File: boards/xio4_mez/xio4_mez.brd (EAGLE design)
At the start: 63 x 91 mm, 55 parts, among them J1 FPGA

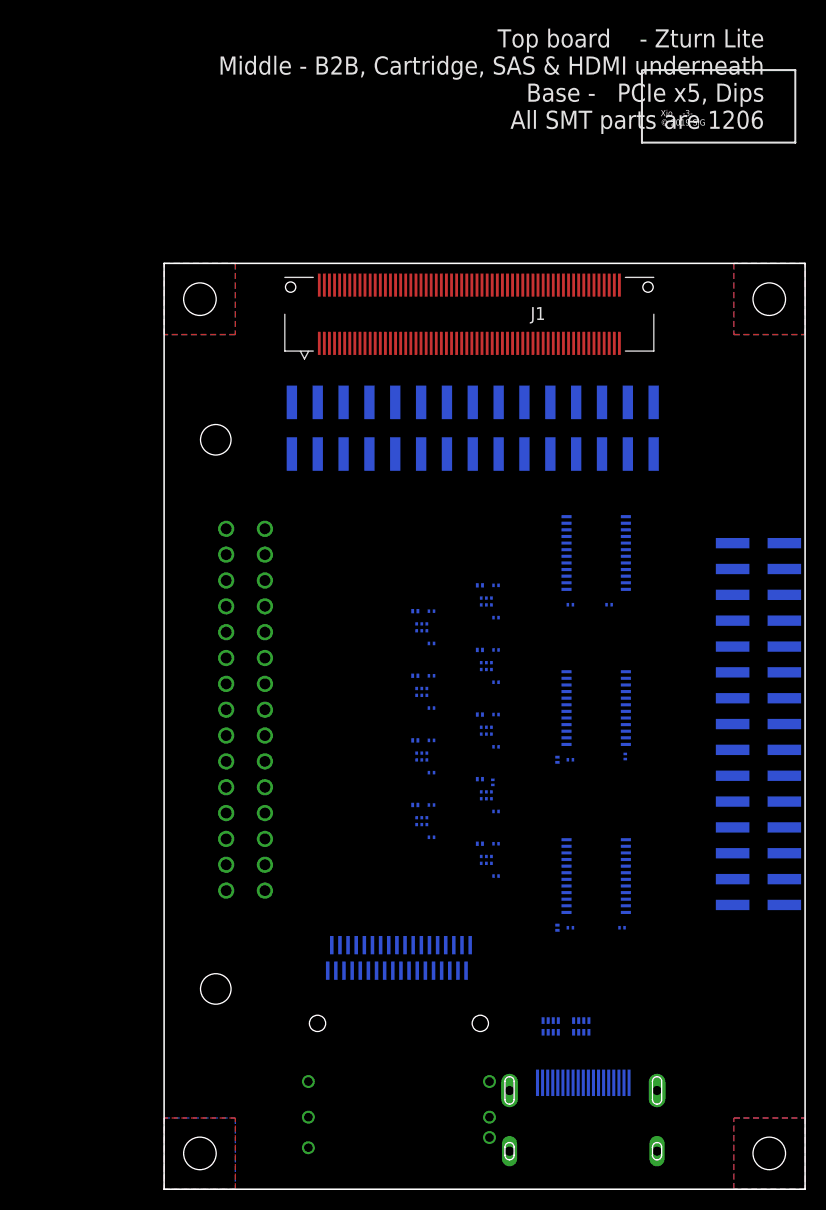
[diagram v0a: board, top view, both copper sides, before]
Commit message: Add the HDMI stage
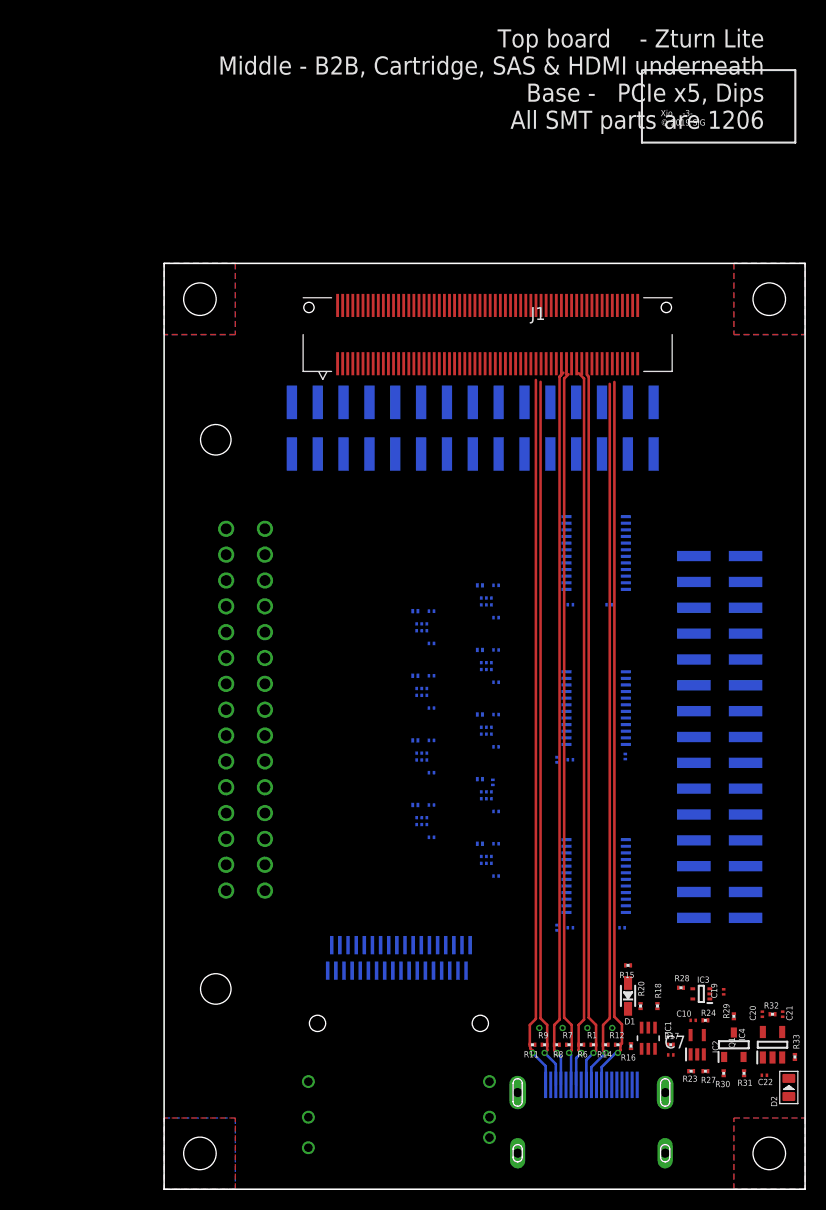
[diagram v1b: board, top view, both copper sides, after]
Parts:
- removed RN1, RN2: 49R9, samacsys:YC124FR0749R9L
- added C10, C19, C20, C21, C22, C7: 0.1uF, rcl:C0201
- added D1: RB751V40,115, microbuilder:SOD-323
- added D2: RED-0805, Seeed-LED:LED-0805
- added IC1: SN74LVC2G07DCKR, samacsys:SOT65P210X110X6N
- added IC2: SN74LVC1G07MDCKREP, samacsys:SOT65P210X110-5N
- added IC3: NL17SZ126XV5T2G, samacsys:SOTFL50P160X60-5N
- added IC4: TPS2051BDBVR, samacsys:SOT95P280X145-5N
- added Q1: SMMBT3904LT1G, samacsys:SOT96P237X111-3N
- added R1, R11, R12, R14, R6, R7, R8, R9: 49R9, rcl:R0201
- added R15: 27K, rcl:R0201
- added R16, R17: 1K5, rcl:R0201
- added R18, R20: 4K7, rcl:R0201
- added R23, R27: 100K, rcl:R0201
- added R24, R28, R30: 1K, rcl:R0201
- added R29, R31, R32: 10K, rcl:R0201
- added R33: 820R, rcl:R0201
- moved JP2 4.02 mm to (55.9, 27.9)
- moved J1 2.69 mm to (31.8, 84.0)
- moved CN1 0.82 mm to (42.0, 10.3)
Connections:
- removed net TX0_SHIELD: CN1.8
- removed net TX1_SHIELD: CN1.5
- removed net TX2_SHIELD: CN1.2
- removed net TXC_SHIELD: CN1.11
- new net HDMI_CEC: CN1.13, D1.C, J1.90
- new net HDMI_DET_IO: IC3.2, J1.84, R24.2, R27.2
- new net HDMI_OUT_EN: J1.80, R30.1, R32.2
- new net HDMI_SCL: IC1.1, J1.88, R18.2
- new net HDMI_SDA: IC1.3, J1.86, R20.2
- new net HPD: CN1.19, IC2.2, R23.2, R28.2
- new net N$1: CN1.16, IC1.6, R17.1
- new net N$10: D2.-, R33.2
- new net N$2: D1.A, R15.1
- new net N$3: CN1.15, IC1.4, R16.1
- new net N$4: IC3.1, Q1.3, R29.2
- new net N$5: IC2.4, R24.1
- new net N$6: IC3.4, R28.1
- new net N$7: Q1.1, R30.2, R31.1
- new net N$8: C21.1, IC4.4, R32.1
- new net N$9: IC4.3, R33.1
- new net V+: C22.1, C7.1, CN1.18, IC4.1, R16.2, R17.2
- net +5V: now also C20.1, IC4.5; no longer CN1.18
- net GND: now also C10.2, C19.2, C20.2, C21.2, C22.2, C7.2, CN1.11, CN1.2, CN1.5, CN1.8, IC1.2, IC2.3, IC3.3, IC4.2, Q1.2, R23.1, R27.1, R31.2
- net TX0_N: now also R1.2; no longer RN1.3
- net TX0_P: now also R6.2; no longer RN1.4
- net TX1_N: now also R7.2; no longer RN2.1
- net TX1_P: now also R8.2; no longer RN2.2
- net TX2_N: now also R9.2; no longer RN2.3
- net TX2_P: now also R11.2; no longer RN2.4
- net TXC_N: now also R12.2; no longer RN1.1
- net TXC_P: now also R14.2; no longer RN1.2
- net VCCIO: now also C10.1, C19.1, D2.+, IC1.5, IC2.5, IC3.5, R1.1, R11.1, R12.1, R14.1, R15.2, R18.1, R20.1, R29.1, R6.1, R7.1, R8.1, R9.1; no longer RN1.5, RN1.6, RN1.7, RN1.8, RN2.5, RN2.6, RN2.7, RN2.8
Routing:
- net TX0_P: track 0.00 -> 70.7 mm, vias 0 -> 1
- net TX1_P: track 0.00 -> 70.6 mm, vias 0 -> 1
- net TX1_N: track 0.00 -> 70.5 mm, vias 0 -> 1
- net TX0_N: track 0.00 -> 70.5 mm, vias 0 -> 1
- net TXC_N: track 0.00 -> 70.3 mm, vias 0 -> 1
- net TX2_P: track 0.00 -> 70.2 mm, vias 0 -> 1
- net TX2_N: track 0.00 -> 69.9 mm, vias 0 -> 1
- net TXC_P: track 0.00 -> 69.9 mm, vias 0 -> 1

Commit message: Use the corrected footprint for the Mezzanine board, and route the HDMI critical signals.
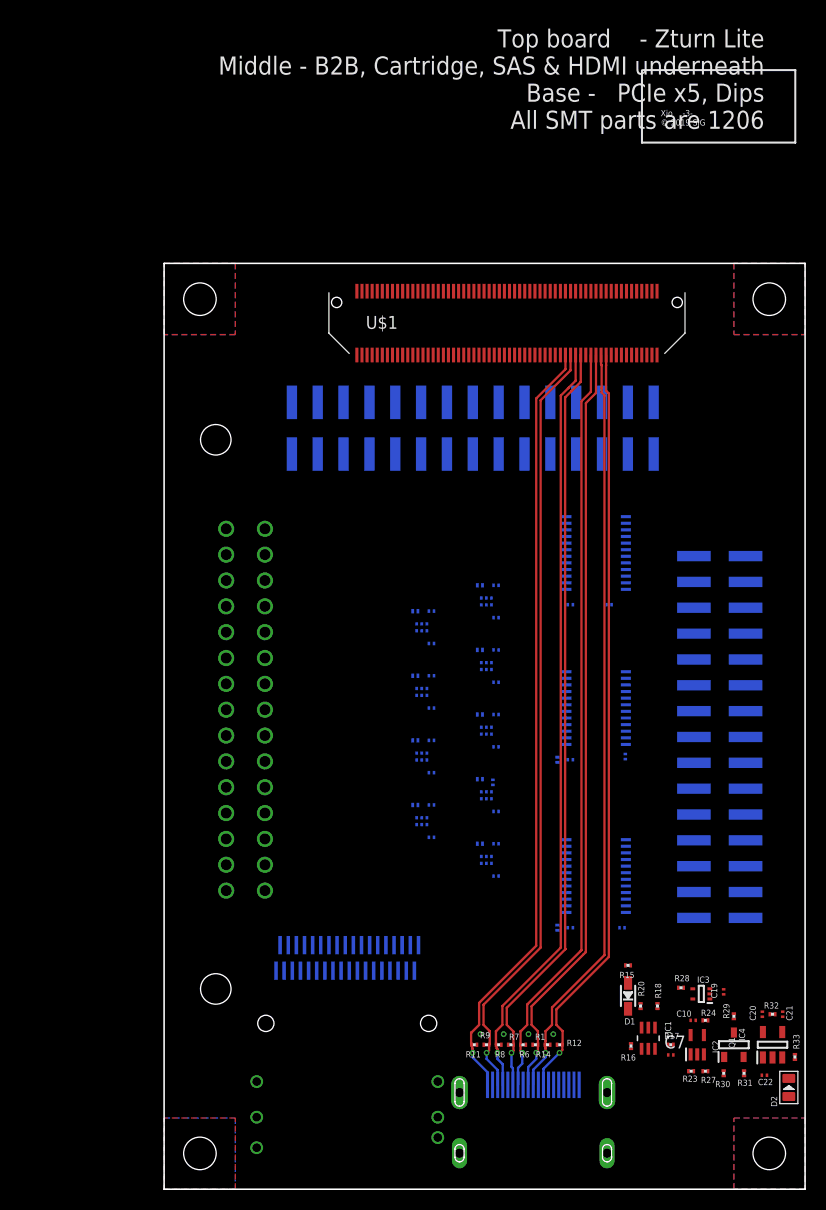
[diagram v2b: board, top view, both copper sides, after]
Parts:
- removed J1: FPGA, pbxl:BSH-060-01-L-D-A
- added U$1: BTH-060-01-F-D-A, pbxl:BTH-060-01-F-D-A
- moved CN1 5.72 mm to (36.3, 10.3)
- moved R1 5.72 mm to (36.5, 14.2)
- moved R11 5.72 mm to (30.5, 14.2)
- moved R12 5.72 mm to (38.9, 14.2)
- moved R6 5.72 mm to (35.3, 14.2)
- moved R8 5.72 mm to (32.9, 14.2)
- moved R9 5.71 mm to (31.7, 14.2)
- moved R14 5.71 mm to (37.7, 14.2)
- moved R7 5.71 mm to (34.1, 14.2)
- moved U$3 5.08 mm to (18.4, 12.7)
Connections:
- net HDMI_CEC: no longer J1.90
- net HDMI_DET_IO: now also U$1.107; no longer J1.84
- net HDMI_OUT_EN: now also U$1.109; no longer J1.80
- net HDMI_SCL: now also U$1.105; no longer J1.88
- net HDMI_SDA: now also U$1.103; no longer J1.86
- net TX0_N: now also U$1.95; no longer J1.106
- net TX0_P: now also U$1.93; no longer J1.104
- net TX1_N: now also U$1.89; no longer J1.100
- net TX1_P: now also U$1.87; no longer J1.98
- net TX2_N: now also U$1.85; no longer J1.96
- net TX2_P: now also U$1.83; no longer J1.94
- net TXC_N: now also U$1.99; no longer J1.110
- net TXC_P: now also U$1.97; no longer J1.108
- net VCCIO: now also U$1.19, U$1.20, U$1.70, U$1.81; no longer J1.19, J1.20, J1.70, J1.81
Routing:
- net TX2_N: track 69.9 -> 76.1 mm
- net TX2_P: track 70.2 -> 76.3 mm
- net TXC_P: track 69.9 -> 74.8 mm
- net TXC_N: track 70.3 -> 75.0 mm
- net TX1_N: track 70.5 -> 75.2 mm
- net TX1_P: track 70.6 -> 75.3 mm
- net TX0_N: track 70.5 -> 75.0 mm
- net TX0_P: track 70.7 -> 74.9 mm

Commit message: Add the SPI routing
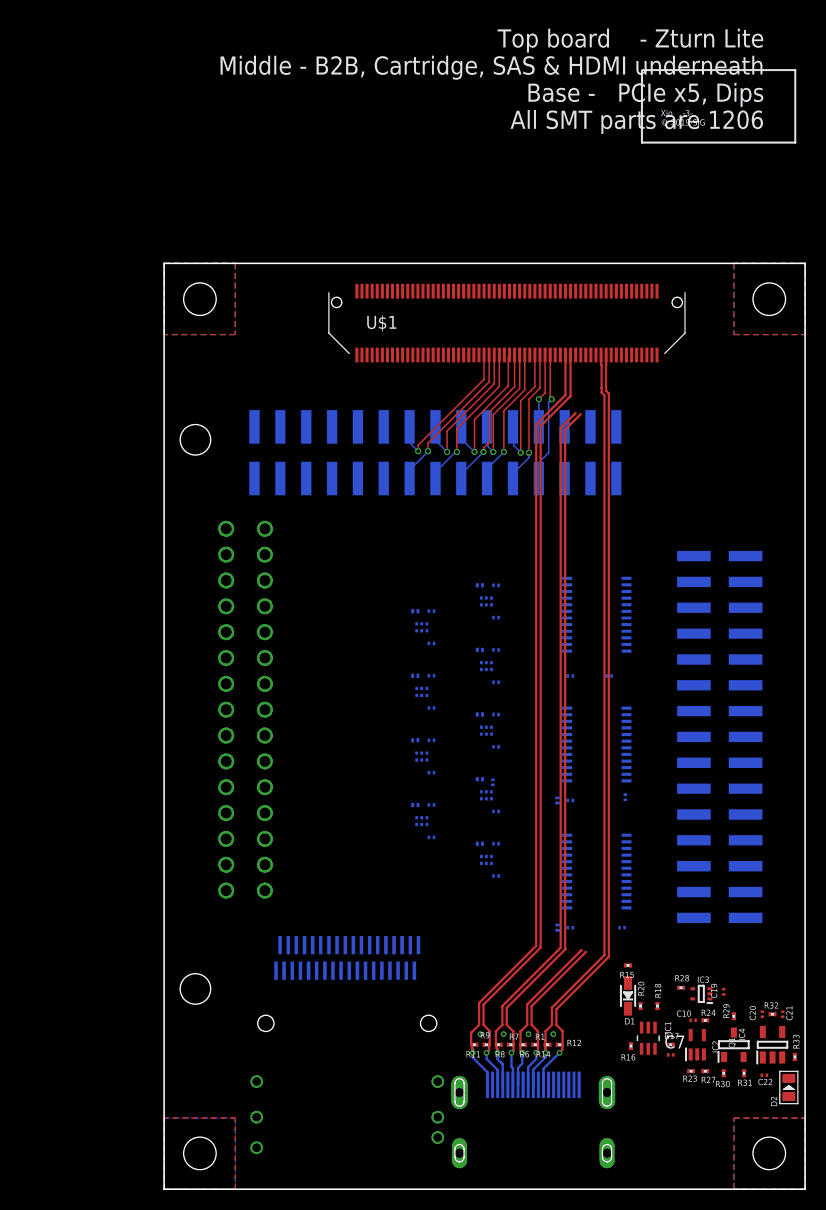
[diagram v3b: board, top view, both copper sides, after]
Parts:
- moved JP2 33.1 mm to (53.3, 61.0), turned to 270 degrees
- moved C15 7.00 mm to (43.7, 50.5)
- moved C3 7.00 mm to (39.9, 50.5)
- moved LVL_ALO 6.06 mm to (42.5, 56.5), turned to 270 degrees
- moved JP1 4.39 mm to (43.2, 73.7)
- moved C13 4.00 mm to (39.9, 38.2)
- moved C18 4.00 mm to (45.3, 38.5)
- moved R25 4.00 mm to (38.7, 38.2)
- moved LVL_D 3.58 mm to (42.5, 43.7), turned to 270 degrees
- moved LVL_AHI 0.44 mm to (42.5, 31.2), turned to 270 degrees
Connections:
- new net SPI0_CLK: JP1.7, U$1.77
- new net SPI0_MISO: JP1.8, U$1.75
- new net SPI0_MOSI: JP1.9, U$1.73
- new net SPI1_CLK: JP1.10, U$1.71
- new net SPI1_MISO: JP1.11, U$1.67
- new net SPI1_MOSI: JP1.12, U$1.65
- new net SPI_SS0: JP1.13, U$1.63
- new net SPI_SS1: JP1.14, U$1.61
- new net SPI_SS2: JP1.15, U$1.57
- new net SPI_SS3: JP1.16, U$1.55
- new net SPI_SS4: JP1.17, U$1.53
- new net SPI_SS5: JP1.18, U$1.51
- net !LO_EXTSEL!: now also JP2.6
- net !LO_HALT!: now also JP2.8
- net !LO_IRQ!: now also JP2.10
- net !LO_MPD!: now also JP2.12
- net !LO_RST!: now also JP1.5
- net GND: now also U$1.101, U$1.102, U$1.111, U$1.112, U$1.113, U$1.17, U$1.18, U$1.29, U$1.30, U$1.39, U$1.40, U$1.49, U$1.50, U$1.59, U$1.60, U$1.69, U$1.7, U$1.72, U$1.79, U$1.8, U$1.82, U$1.91, U$1.92
- net LO_A0: now also JP2.1
- net LO_A1: now also JP2.3
- net LO_A10: now also JP2.21
- net LO_A11: now also JP2.23
- net LO_A12: now also JP2.25
- net LO_A13: now also JP2.27
- net LO_A14: now also JP2.29
- net LO_A15: now also JP2.30
- net LO_A2: now also JP2.5
- net LO_A3: now also JP2.7
- net LO_A4: now also JP2.9
- net LO_A5: now also JP2.11
- net LO_A6: now also JP2.13
- net LO_A7: now also JP2.15
- net LO_A8: now also JP2.17
- net LO_A9: now also JP2.19
- net LO_CLK: now also JP2.2
- net LO_D0: now also JP2.14
- net LO_D1: now also JP2.16
- net LO_D2: now also JP2.18
- net LO_D3: now also JP2.20
- net LO_D4: now also JP2.22
- net LO_D5: now also JP2.24
- net LO_D6: now also JP2.26
- net LO_D7: now also JP2.28
- net LO_R/!W!: now also JP2.4
- net LO_RD4: now also JP1.1
- net LO_RD5: now also JP1.3
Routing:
- net TX0_N: track 75.0 -> 15.9 mm
- net TX0_P: track 74.9 -> 16.0 mm
- net SPI_SS4: track 0.00 -> 15.4 mm, vias 0 -> 1
- net SPI_SS5: track 0.00 -> 14.9 mm, vias 0 -> 1
- net SPI_SS2: track 0.00 -> 14.8 mm, vias 0 -> 1
- net SPI_SS3: track 0.00 -> 14.4 mm, vias 0 -> 1
- net SPI_SS0: track 0.00 -> 14.3 mm, vias 0 -> 1
- net SPI_SS1: track 0.00 -> 13.9 mm, vias 0 -> 1
- net SPI1_MISO: track 0.00 -> 13.7 mm, vias 0 -> 1
- net SPI1_MOSI: track 0.00 -> 13.3 mm, vias 0 -> 1
- net SPI0_MOSI: track 0.00 -> 13.2 mm, vias 0 -> 1
- net SPI1_CLK: track 0.00 -> 13.0 mm, vias 0 -> 1
- net SPI0_CLK: track 0.00 -> 12.7 mm, vias 0 -> 1
- net SPI0_MISO: track 0.00 -> 7.32 mm, vias 0 -> 1
- net TX1_N: track 75.2 -> 69.4 mm
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
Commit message: First pass at a “finished” board
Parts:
- added JP3: (no value), pinhead-2:2X15SMD
- moved U$17 7.75 mm to (31.7, 31.7)
- moved C63 7.75 mm to (32.6, 30.1)
- moved C68 7.75 mm to (32.6, 33.3)
- moved R21 7.75 mm to (31.0, 33.3)
- moved U$16 7.10 mm to (31.7, 58.4)
- moved C11 7.10 mm to (32.6, 60.0)
- moved R10 7.10 mm to (31.0, 60.0)
- moved C4 7.10 mm to (32.6, 56.8)
- moved U$4 6.63 mm to (31.7, 40.6)
- moved C5 6.63 mm to (32.6, 39.0)
- moved C8 6.63 mm to (32.6, 42.2)
- moved R5 6.63 mm to (31.0, 42.2)
- moved U$14 6.38 mm to (31.7, 49.5)
- moved C12 6.38 mm to (32.6, 51.1)
- moved C65 6.38 mm to (32.6, 47.9)
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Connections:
- new net HBUS0: JP3.2, U$1.22
- new net HBUS1: JP3.1, U$1.24
- new net HBUS10: JP3.12, U$1.46
- new net HBUS11: JP3.11, U$1.48
- new net HBUS12: JP3.14, U$1.52
- new net HBUS13: JP3.13, U$1.54
- new net HBUS14: JP3.16, U$1.56
- new net HBUS15: JP3.15, U$1.58
- new net HBUS16: JP3.18, U$1.62
- new net HBUS17: JP3.17, U$1.64
- new net HBUS18: JP3.20, U$1.66
- new net HBUS19: JP3.19, U$1.68
- new net HBUS2: JP3.4, U$1.26
- new net HBUS20: JP3.22, U$1.74
- new net HBUS21: JP3.21, U$1.76
- new net HBUS22: JP3.24, U$1.78
- new net HBUS23: JP3.23, U$1.80
- new net HBUS24: JP3.26, U$1.84
- new net HBUS25: JP3.25, U$1.86
- new net HBUS26: JP3.28, U$1.88
- new net HBUS27: JP3.27, U$1.90
- new net HBUS3: JP3.3, U$1.28
- new net HBUS4: JP3.6, U$1.32
- new net HBUS5: JP3.5, U$1.34
- new net HBUS6: JP3.8, U$1.36
- new net HBUS7: JP3.7, U$1.38
- new net HBUS8: JP3.10, U$1.42
- new net HBUS9: JP3.9, U$1.44
- new net PRESENT0: JP1.25, U$1.16
- new net PRESENT1: JP1.26, U$1.14
- new net PRESENT2: JP1.27, U$1.12
- new net PRESENT3: JP1.28, U$1.10
- new net PRESENT4: JP1.29, U$1.6
- new net PRESENT5: JP1.30, U$1.4
- new net SPI_IRQ0: JP1.19, U$1.47
- new net SPI_IRQ1: JP1.20, U$1.45
- new net SPI_IRQ2: JP1.21, U$1.43
- new net SPI_IRQ3: JP1.22, U$1.41
- new net SPI_IRQ4: JP1.23, U$1.37
- new net SPI_IRQ5: JP1.24, U$1.35
- new net VALID_RD: JP1.4, U$1.110
- new net VALID_WR: JP1.6, U$1.108
- net +5V: now also JP1.2, JP3.29, JP3.30
- net DIR_A: now also U$1.33
- net DIR_CLK: now also U$1.27
- net DIR_D: now also U$1.31
- net DIR_EXTSEL: now also U$1.25
- net DIR_HALT: now also U$1.23
- net DIR_IRQ: now also U$1.21
- net DIR_MPD: now also U$1.15
- net DIR_RD4: now also U$1.13
- net DIR_RD5: now also U$1.11
- net DIR_RST: now also U$1.9
- net DIR_RW: now also U$1.5
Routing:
- net TX0_N: track 15.9 -> 75.0 mm
- net TX0_P: track 16.0 -> 74.9 mm
- net TX1_N: track 69.4 -> 75.2 mm
- net TX1_P: track 69.6 -> 75.3 mm
